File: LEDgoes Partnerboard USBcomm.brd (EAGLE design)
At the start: 36.8 x 53.3 mm, 22 parts, among them SW1 POWER, SW2 RESET

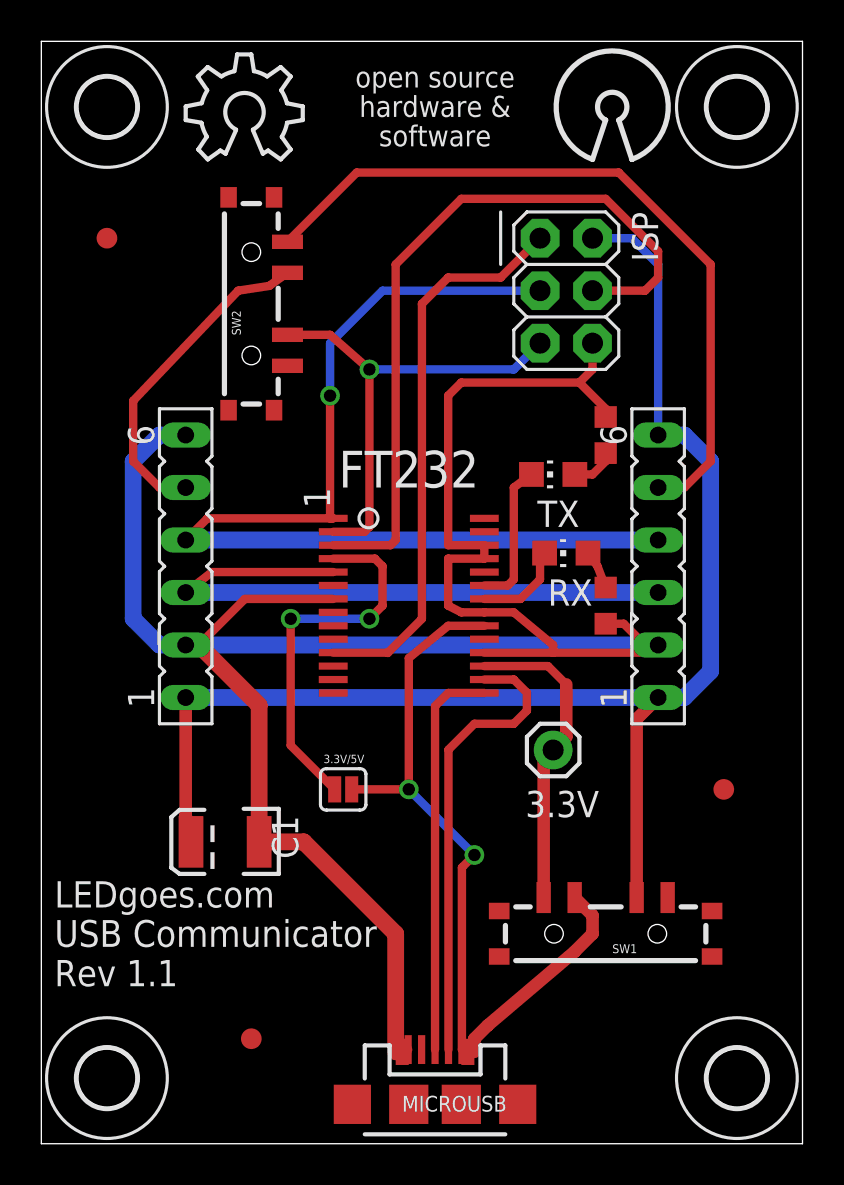
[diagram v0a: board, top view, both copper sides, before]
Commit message: Slight changes made to Rev 1 before production
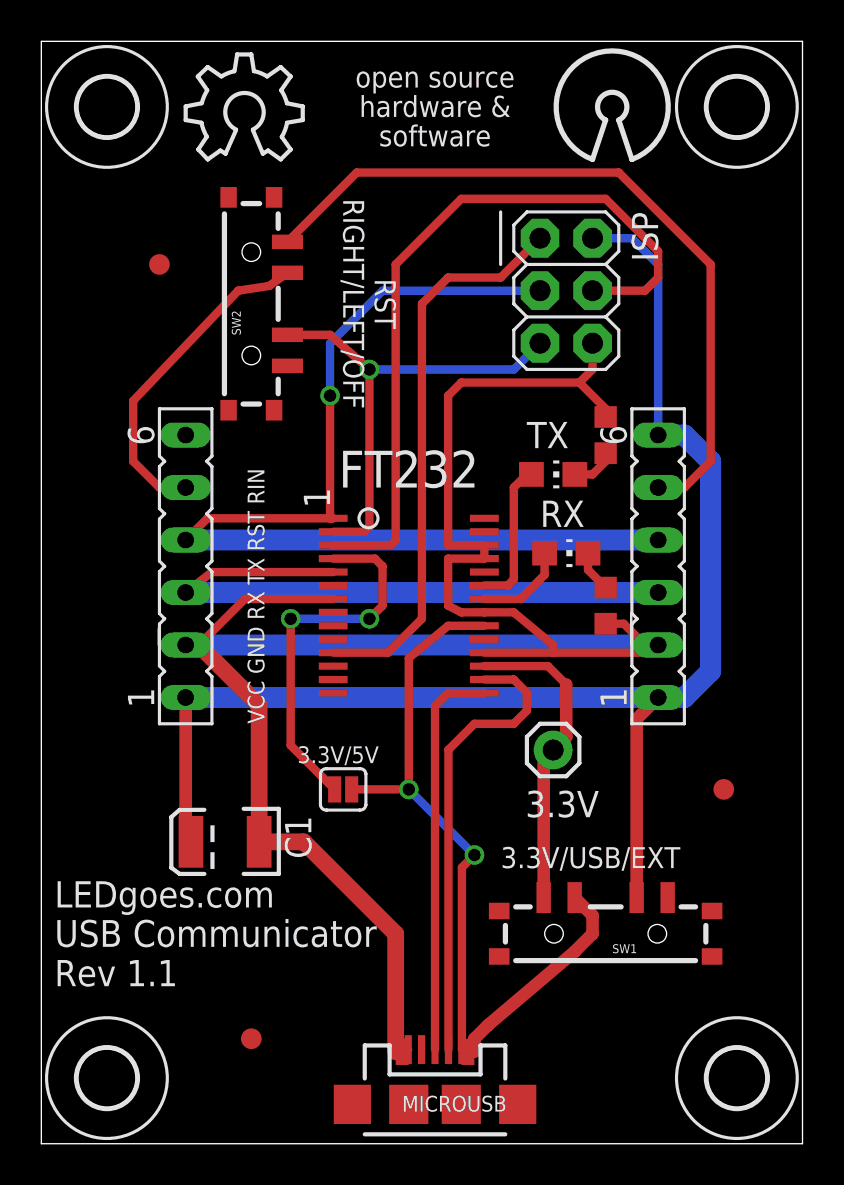
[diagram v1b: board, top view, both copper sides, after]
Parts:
- moved E$6 2.84 mm to (8.26, 45.1)
- turned RX to 270 degrees
- turned TX to 270 degrees
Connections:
- removed net S$6: R1.1, TX.A
- new net S$20: R1.1, TX.C
- net S$1: no longer _.6
- net S$19: now also RX.C; no longer RX.A
- net S$3: now also TX.A; no longer TX.C
- net S$5: now also RX.A; no longer RX.C
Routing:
- net S$1: track 112.5 -> 98.7 mm
- net S$6: track 2.15 -> 0.00 mm
- net S$20: track 0.00 -> 2.15 mm
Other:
- board text added: "3.3V/USB/EXT"
- board text added: "RST RIGHT/LEFT/OFF"
